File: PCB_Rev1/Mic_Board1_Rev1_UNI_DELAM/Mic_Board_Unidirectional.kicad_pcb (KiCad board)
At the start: 2 copper layers, 51 x 31.5 mm, 29 parts, among them J2 532610771, J3 S2B-ZR-SM4A-TF_LF__SN_, U1 OPA1671IDBVR

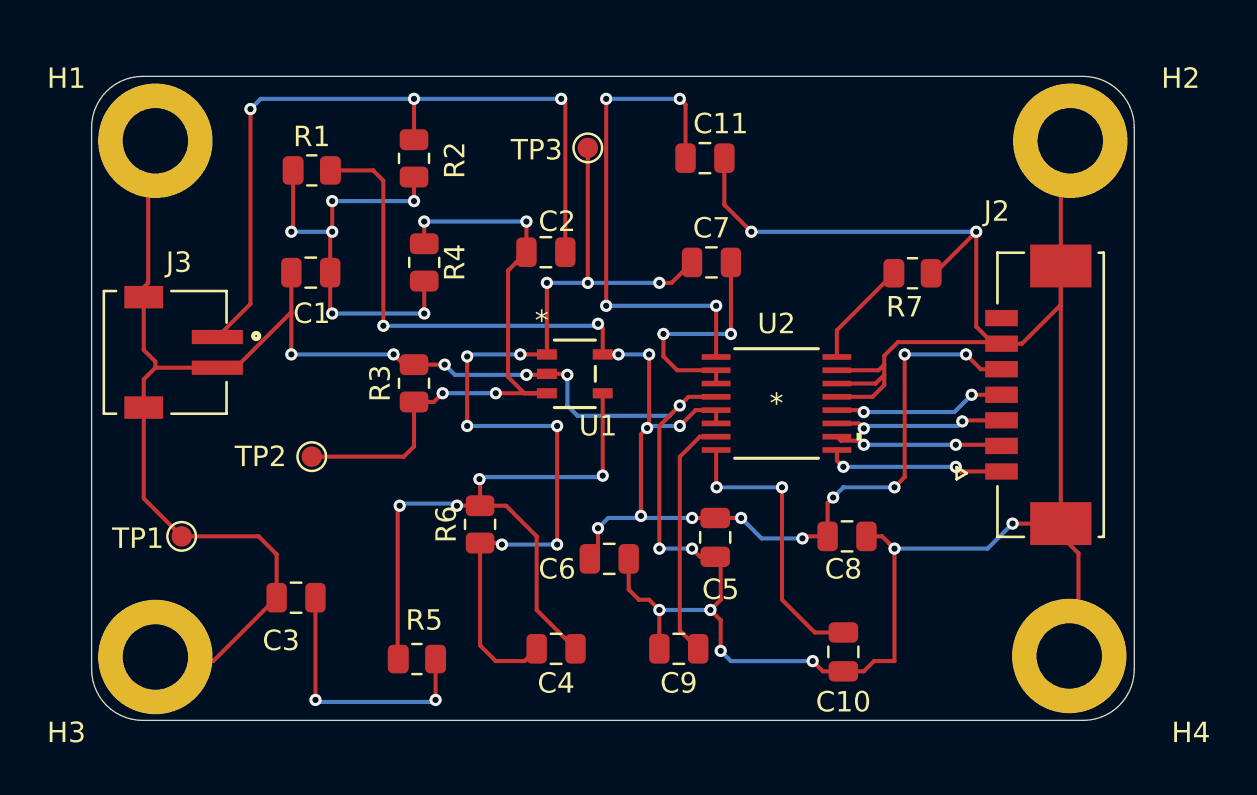
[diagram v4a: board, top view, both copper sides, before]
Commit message: Mic Board silkscreen complete
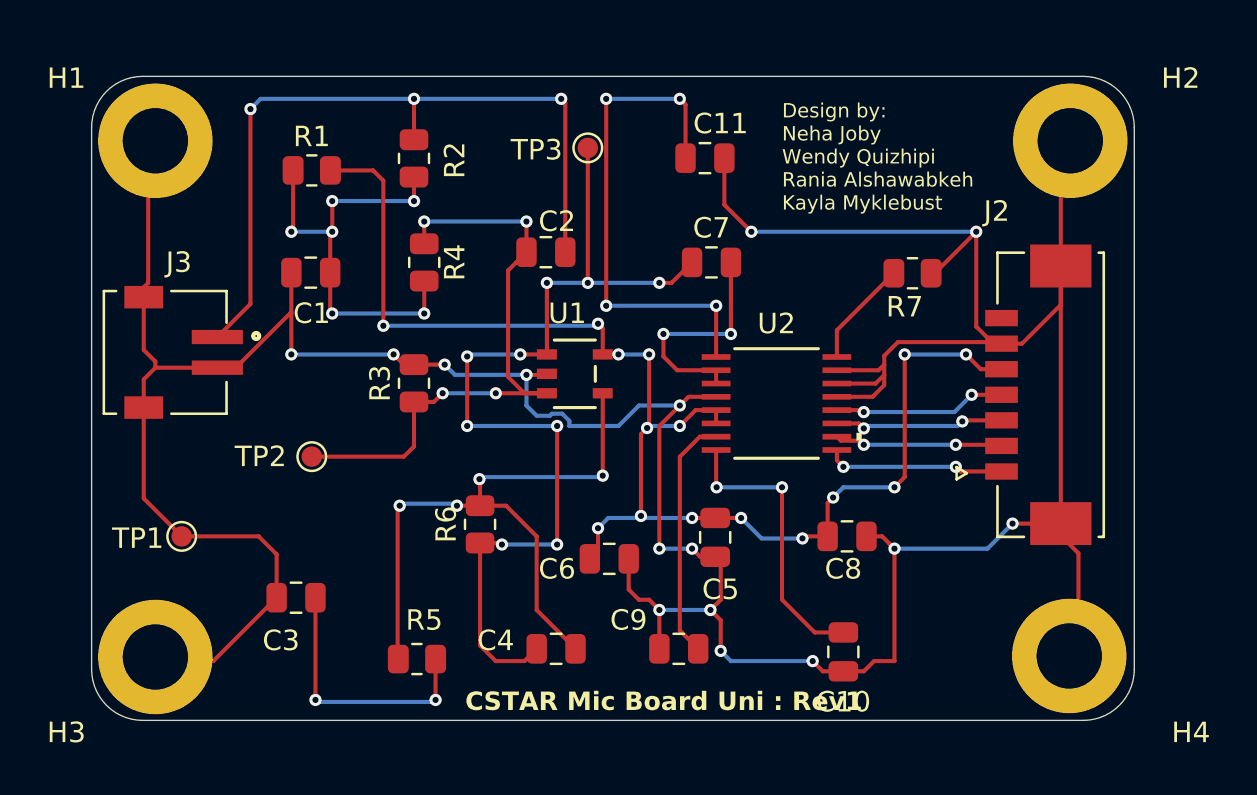
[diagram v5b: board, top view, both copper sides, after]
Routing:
- net GND: track 190.2 -> 191.8 mm, vias 16 -> 15
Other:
- board text added: "CSTAR Mic Board Uni : Rev1"
- board text added: "Design by: Neha Joby Wendy Quizhipi Rania Alshawabkeh Kayla Myklebust"

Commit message: Audio Connector Pins
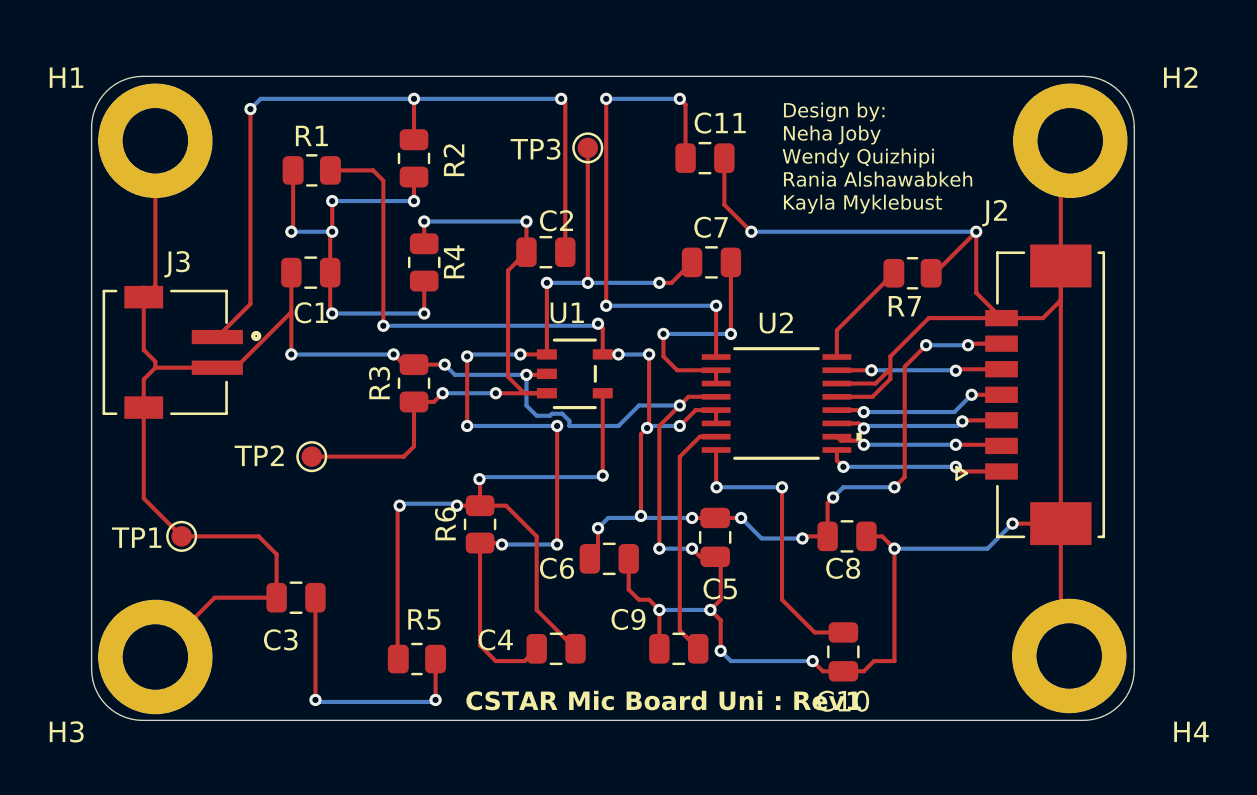
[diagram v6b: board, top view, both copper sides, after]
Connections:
- J2 pad 5: +3V3 -> Net-(U2-FSEL)
- J2 pad 6: GND -> +3V3
- J2 pad 7: unconnected-(J2-Pad7) -> GND
- U2 pad 15: GND -> Net-(U2-FSEL)
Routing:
- net Net-(U2-FSEL): track 0.00 -> 8.09 mm, vias 0 -> 2
- net GND: track 191.8 -> 188.8 mm

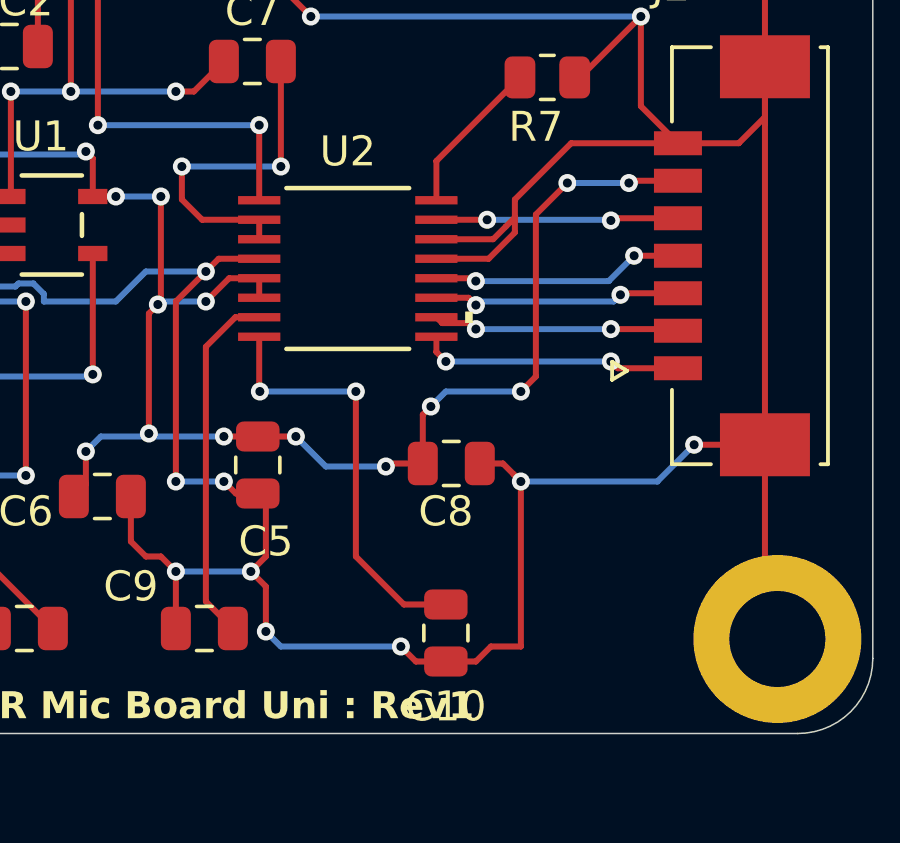
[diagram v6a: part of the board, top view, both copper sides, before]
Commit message: Connections Adjustments
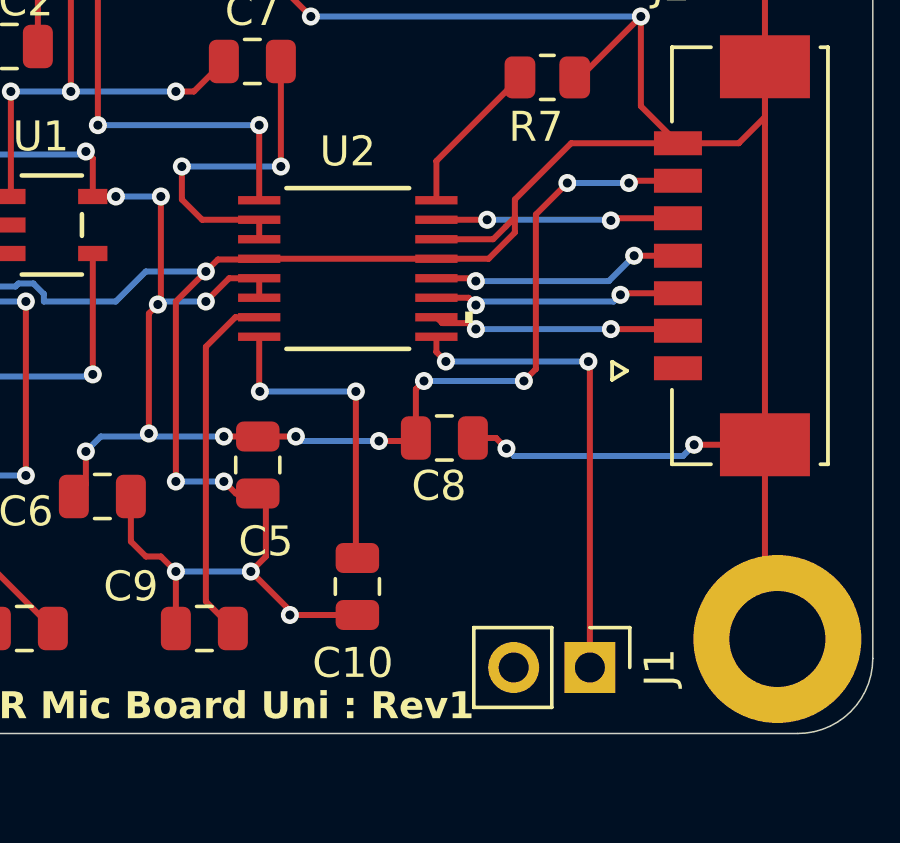
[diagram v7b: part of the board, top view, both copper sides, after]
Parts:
- added J1: Conn_01x02_Pin, Connector_PinHeader_2.54mm:PinHeader_1x02_P2.54mm_Vertical, F.Cu at (169.8, 95.2)
- moved C10 3.33 mm to (162.1, 92.5)
- moved C8 0.88 mm to (164.9, 87.5)
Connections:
- J2 pad 1: Net-(U2-SDTO) -> unconnected-(J2-Pad1)
- U2 pad 9: Net-(U2-SDTO) -> Net-(J1-Pin_1)
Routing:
- net Net-(J1-Pin_1): track 0.00 -> 15.9 mm, vias 0 -> 2
- net Net-(U2-SDTO): track 8.79 -> 0.00 mm, vias 2 -> 0
- net GND: track 188.8 -> 182.4 mm, vias 15 -> 14
- net Net-(U2-REGO): track 14.2 -> 10.5 mm
